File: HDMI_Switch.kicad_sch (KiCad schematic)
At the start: 16 parts, among them U7 HD3SS215RTQR

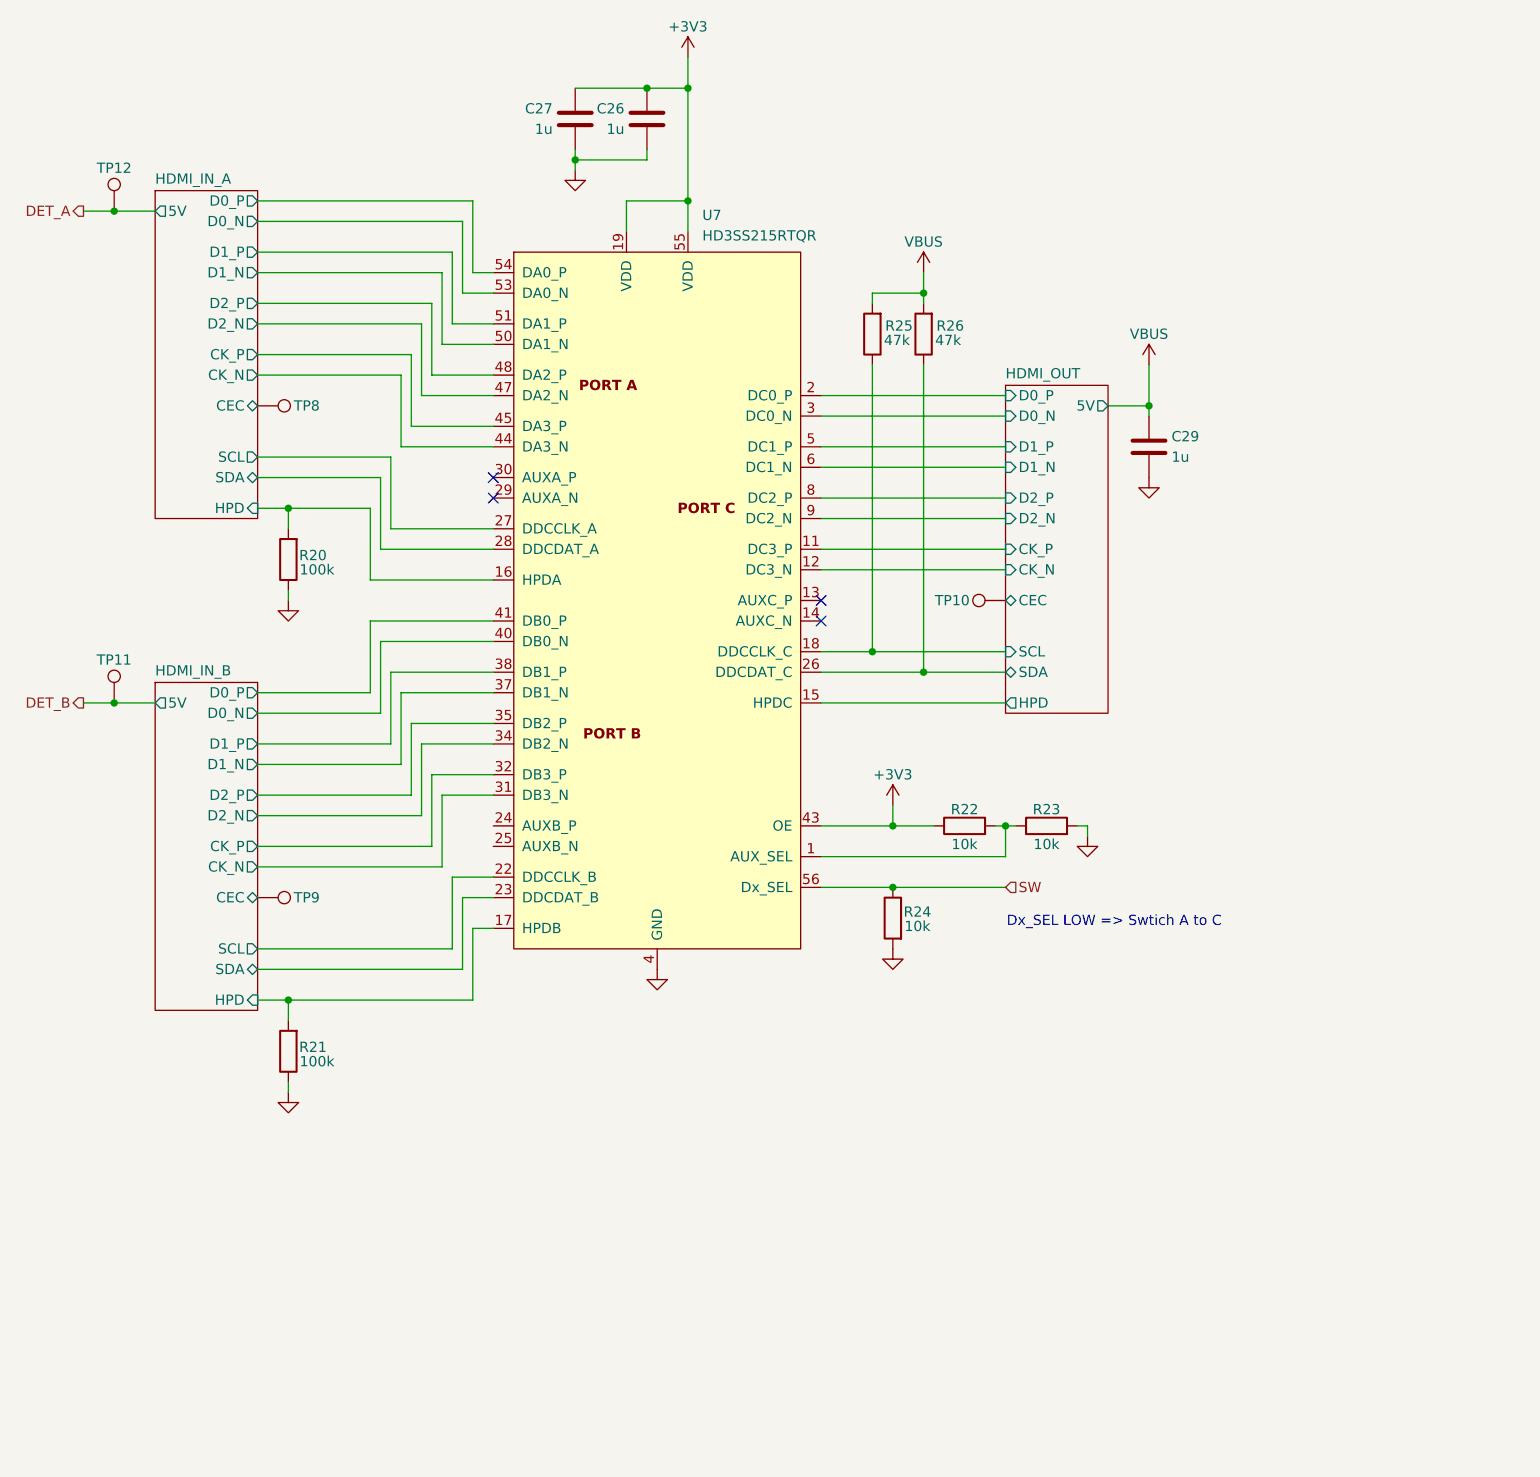
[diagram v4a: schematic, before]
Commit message: Fixed DRC & Adnotations
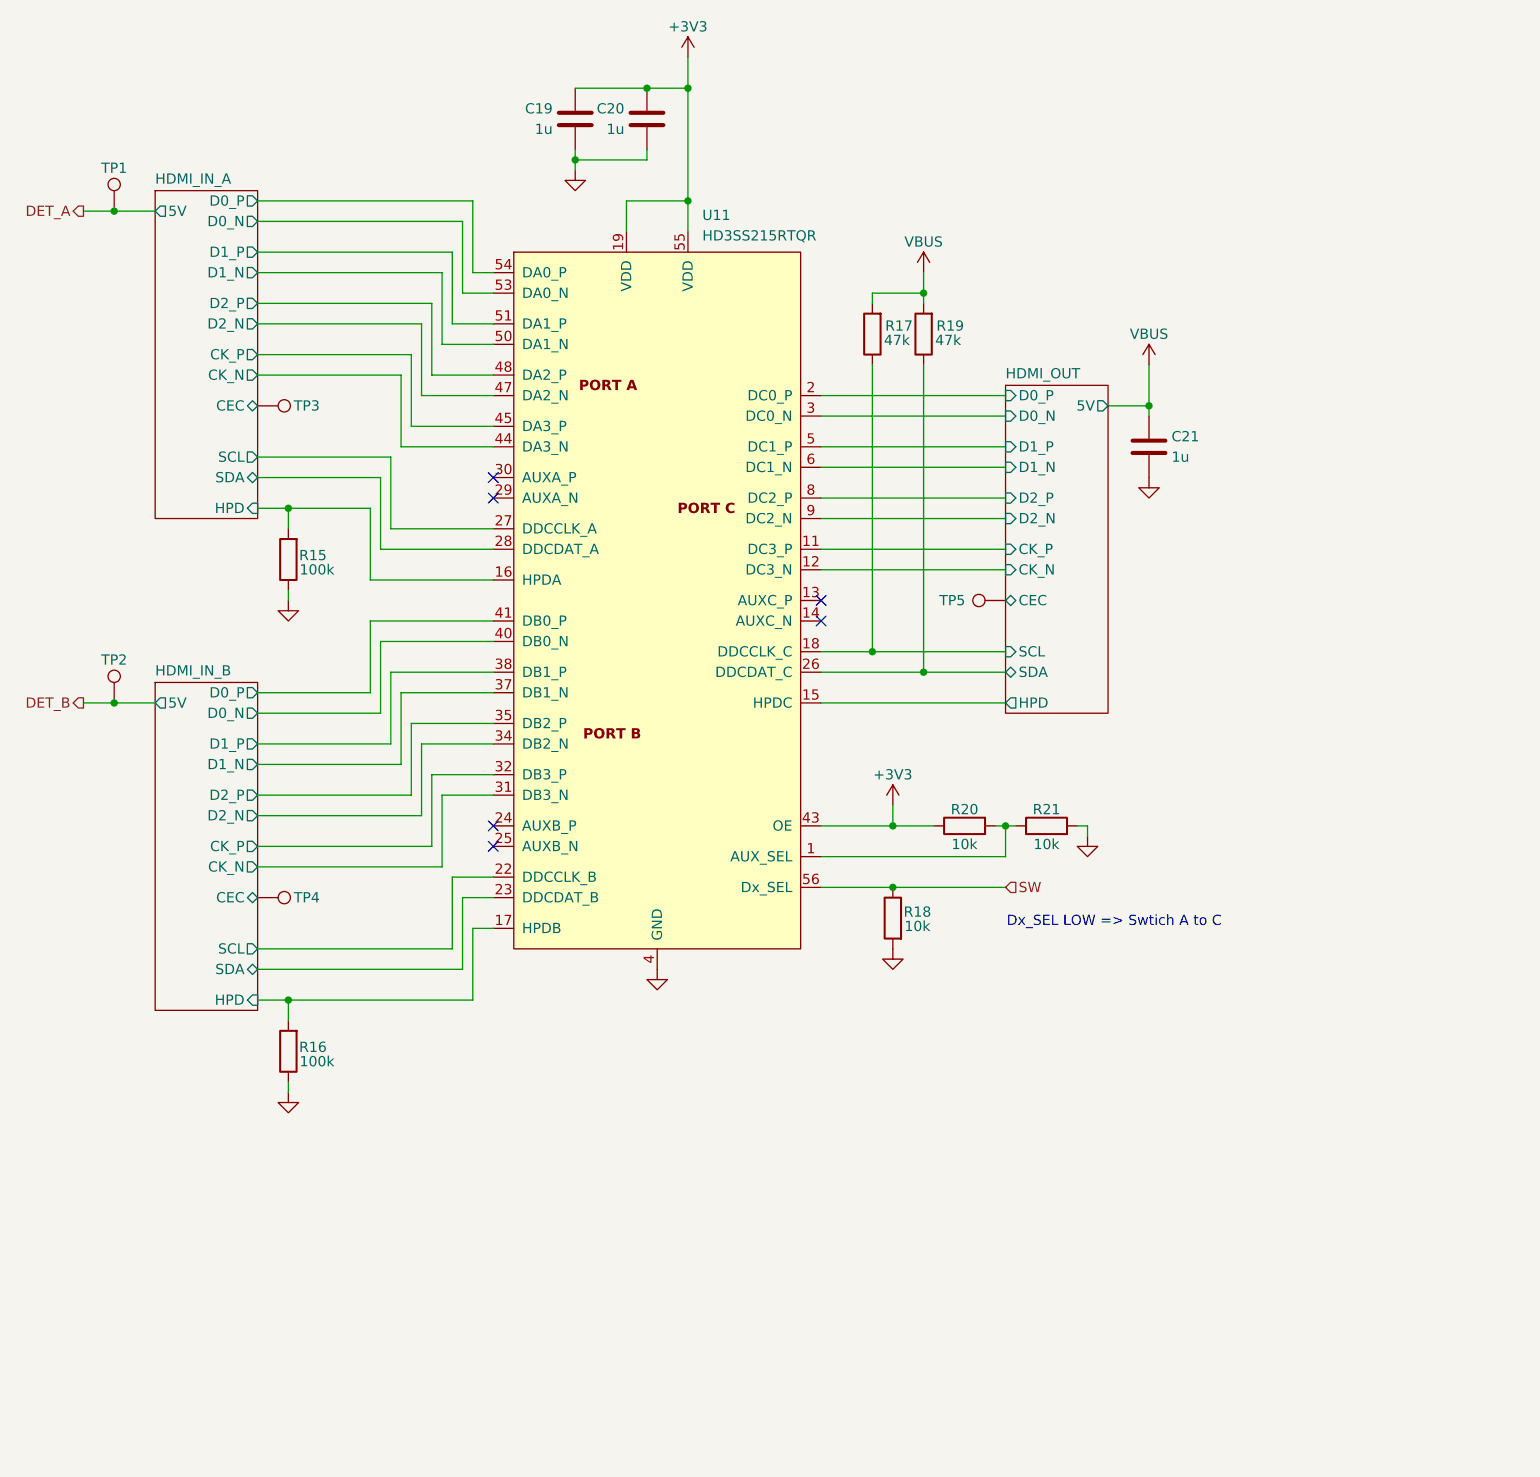
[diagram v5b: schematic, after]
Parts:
- renumbered C27 to C19, C26 to C20, C29 to C21, R20 to R15, R21 to R16, R25 to R17, R24 to R18, R26 to R19, R22 to R20, R23 to R21, TP12 to TP1, TP11 to TP2, TP8 to TP3, TP9 to TP4, TP10 to TP5, U7 to U11
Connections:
- no-connect marks 4 -> 6
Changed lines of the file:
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@@
 	)
 	(no_connect
+		(at 118.11 124.46)
+	)
+	(no_connect
 		(at 158.75 96.52)
 	)
@@
 		(at 158.75 99.06)
 	)
+	(no_connect
+		(at 118.11 127)
+	)
 	(wire
 		(pts
@@
 		(in_pos_files yes)
 		(dnp no)
-		(property "Reference" "#PWR054"
+		(property "Reference" "#PWR027"
 			(at 142.24 33.02 0)
 			(hide yes)
@@
 			(project "KVM_Switch"
 				(path "/94386106-ccd4-487f-b5c5-d52ec3dd59db/6e43926c-16e0-4a92-a7fc-ce5a89c8ce59"
-					(reference "#PWR054")
+					(reference "#PWR027")
 					(unit 1)
 				)
@@
 		(in_pos_files yes)
 		(dnp no)
-		(property "Reference" "C27"
+		(property "Reference" "C19"
 			(at 125.476 35.56 0)
 			(show_name no)
@@
 			(project "KVM_Switch"
 				(path "/94386106-ccd4-487f-b5c5-d52ec3dd59db/6e43926c-16e0-4a92-a7fc-ce5a89c8ce59"
-					(reference "C27")
+					(reference "C19")
 					(unit 1)
 				)
@@
 		(in_pos_files yes)
 		(dnp no)
-		(property "Reference" "C29"
+		(property "Reference" "C21"
 			(at 202.184 76.2 0)
 			(show_name no)
@@
 			(project "KVM_Switch"
 				(path "/94386106-ccd4-487f-b5c5-d52ec3dd59db/6e43926c-16e0-4a92-a7fc-ce5a89c8ce59"
-					(reference "C29")
+					(reference "C21")
 					(unit 1)
 				)
@@
 		(in_pos_files yes)
 		(dnp no)
-		(property "Reference" "TP12"
+		(property "Reference" "TP1"
 			(at 71.12 42.926 0)
 			(show_name no)
@@
 			(project "KVM_Switch"
 				(path "/94386106-ccd4-487f-b5c5-d52ec3dd59db/6e43926c-16e0-4a92-a7fc-ce5a89c8ce59"
-					(reference "TP12")
+					(reference "TP1")
 					(unit 1)
 				)
@@
 		(in_pos_files yes)
 		(dnp no)
-		(property "Reference" "R24"
+		(property "Reference" "R18"
 			(at 170.688 135.128 0)
 			(show_name no)
@@
 			(project "KVM_Switch"
 				(path "/94386106-ccd4-487f-b5c5-d52ec3dd59db/6e43926c-16e0-4a92-a7fc-ce5a89c8ce59"
-					(reference "R24")
+					(reference "R18")
 					(unit 1)
 				)
@@
 		(in_pos_files yes)
 		(dnp no)
-		(property "Reference" "#PWR078"
+		(property "Reference" "#PWR031"
 			(at 191.77 132.08 0)
 			(hide yes)
@@
 			(project "KVM_Switch"
 				(path "/94386106-ccd4-487f-b5c5-d52ec3dd59db/6e43926c-16e0-4a92-a7fc-ce5a89c8ce59"
-					(reference "#PWR078")
+					(reference "#PWR031")
 					(unit 1)
 				)
@@
 		(in_pos_files yes)
 		(dnp no)
-		(property "Reference" "#PWR080"
+		(property "Reference" "#PWR033"
 			(at 199.39 87.63 0)
 			(hide yes)
@@
 			(project "KVM_Switch"
 				(path "/94386106-ccd4-487f-b5c5-d52ec3dd59db/6e43926c-16e0-4a92-a7fc-ce5a89c8ce59"
-					(reference "#PWR080")
+					(reference "#PWR033")
 					(unit 1)
 				)
@@
 		(in_pos_files yes)
 		(dnp no)
-		(property "Reference" "TP11"
+		(property "Reference" "TP2"
 			(at 71.12 103.886 0)
 			(show_name no)
@@
 			(project "KVM_Switch"
 				(path "/94386106-ccd4-487f-b5c5-d52ec3dd59db/6e43926c-16e0-4a92-a7fc-ce5a89c8ce59"
-					(reference "TP11")
+					(reference "TP2")
 					(unit 1)
 				)
@@
 		(in_pos_files yes)
 		(dnp no)
-		(property "Reference" "#PWR079"
+		(property "Reference" "#PWR029"
 			(at 167.64 146.05 0)
 			(hide yes)
@@
 			(project "KVM_Switch"
 				(path "/94386106-ccd4-487f-b5c5-d52ec3dd59db/6e43926c-16e0-4a92-a7fc-ce5a89c8ce59"
-					(reference "#PWR079")
+					(reference "#PWR029")
 					(unit 1)
 				)
@@
 		(in_pos_files yes)
 		(dnp no)
-		(property "Reference" "#PWR057"
+		(property "Reference" "#PWR030"
 			(at 171.45 59.69 0)
 			(hide yes)
@@
 			(project "KVM_Switch"
 				(path "/94386106-ccd4-487f-b5c5-d52ec3dd59db/6e43926c-16e0-4a92-a7fc-ce5a89c8ce59"
-					(reference "#PWR057")
+					(reference "#PWR030")
 					(unit 1)
 				)
@@
 		(in_pos_files yes)
 		(dnp no)
-		(property "Reference" "TP10"
+		(property "Reference" "TP5"
 			(at 175.006 96.52 90)
 			(show_name no)
@@
 			(project "KVM_Switch"
 				(path "/94386106-ccd4-487f-b5c5-d52ec3dd59db/6e43926c-16e0-4a92-a7fc-ce5a89c8ce59"
-					(reference "TP10")
+					(reference "TP5")
 					(unit 1)
 				)
@@
 		(in_pos_files yes)
 		(dnp no)
-		(property "Reference" "#PWR073"
+		(property "Reference" "#PWR026"
 			(at 138.43 148.59 0)
 			(hide yes)
@@
 			(project "KVM_Switch"
 				(path "/94386106-ccd4-487f-b5c5-d52ec3dd59db/6e43926c-16e0-4a92-a7fc-ce5a89c8ce59"
-					(reference "#PWR073")
+					(reference "#PWR026")
 					(unit 1)
 				)
@@
 		(in_pos_files yes)
 		(dnp no)
-		(property "Reference" "#PWR072"
+		(property "Reference" "#PWR024"
 			(at 92.71 163.83 0)
 			(hide yes)
@@
 			(project "KVM_Switch"
 				(path "/94386106-ccd4-487f-b5c5-d52ec3dd59db/6e43926c-16e0-4a92-a7fc-ce5a89c8ce59"
-					(reference "#PWR072")
+					(reference "#PWR024")
 					(unit 1)
 				)
@@
 		(in_pos_files yes)
 		(dnp no)
-		(property "Reference" "TP9"
+		(property "Reference" "TP4"
 			(at 94.996 133.35 90)
 			(show_name no)
@@
 			(project "KVM_Switch"
 				(path "/94386106-ccd4-487f-b5c5-d52ec3dd59db/6e43926c-16e0-4a92-a7fc-ce5a89c8ce59"
-					(reference "TP9")
+					(reference "TP4")
 					(unit 1)
 				)
@@
 		(in_pos_files yes)
 		(dnp no)
-		(property "Reference" "R20"
+		(property "Reference" "R15"
 			(at 95.758 90.932 0)
 			(show_name no)
@@
 			(project "KVM_Switch"
 				(path "/94386106-ccd4-487f-b5c5-d52ec3dd59db/6e43926c-16e0-4a92-a7fc-ce5a89c8ce59"
-					(reference "R20")
+					(reference "R15")
 					(unit 1)
 				)
@@
 		(in_pos_files yes)
 		(dnp no)
-		(property "Reference" "#PWR074"
+		(property "Reference" "#PWR025"
 			(at 128.27 49.53 0)
 			(hide yes)
@@
 			(project "KVM_Switch"
 				(path "/94386106-ccd4-487f-b5c5-d52ec3dd59db/6e43926c-16e0-4a92-a7fc-ce5a89c8ce59"
-					(reference "#PWR074")
+					(reference "#PWR025")
 					(unit 1)
 				)
@@
 		(in_pos_files yes)
 		(dnp no)
-		(property "Reference" "R21"
+		(property "Reference" "R16"
 			(at 95.758 151.892 0)
 			(show_name no)
@@
 			(project "KVM_Switch"
 				(path "/94386106-ccd4-487f-b5c5-d52ec3dd59db/6e43926c-16e0-4a92-a7fc-ce5a89c8ce59"
-					(reference "R21")
+					(reference "R16")
 					(unit 1)
 				)
@@
 		(in_pos_files yes)
 		(dnp no)
-		(property "Reference" "R23"
+		(property "Reference" "R21"
 			(at 186.69 122.428 90)
 			(show_name no)
@@
 			(project "KVM_Switch"
 				(path "/94386106-ccd4-487f-b5c5-d52ec3dd59db/6e43926c-16e0-4a92-a7fc-ce5a89c8ce59"
-					(reference "R23")
+					(reference "R21")
 					(unit 1)
 				)
@@
 		(in_pos_files yes)
 		(dnp no)
-		(property "Reference" "U7"
+		(property "Reference" "U11"
 			(at 144.018 48.768 0)
 			(show_name no)
@@
 			(project "KVM_Switch"
 				(path "/94386106-ccd4-487f-b5c5-d52ec3dd59db/6e43926c-16e0-4a92-a7fc-ce5a89c8ce59"
-					(reference "U7")
+					(reference "U11")
 					(unit 1)
 				)
@@
 		(in_pos_files yes)
 		(dnp no)
-		(property "Reference" "TP8"
+		(property "Reference" "TP3"
 			(at 94.996 72.39 90)
 			(show_name no)
@@
 			(project "KVM_Switch"
 				(path "/94386106-ccd4-487f-b5c5-d52ec3dd59db/6e43926c-16e0-4a92-a7fc-ce5a89c8ce59"
-					(reference "TP8")
+					(reference "TP3")
 					(unit 1)
 				)
@@
 		(in_pos_files yes)
 		(dnp no)
-		(property "Reference" "#PWR055"
+		(property "Reference" "#PWR032"
 			(at 199.39 71.12 0)
 			(hide yes)
@@
 			(project "KVM_Switch"
 				(path "/94386106-ccd4-487f-b5c5-d52ec3dd59db/6e43926c-16e0-4a92-a7fc-ce5a89c8ce59"
-					(reference "#PWR055")
+					(reference "#PWR032")
 					(unit 1)
 				)
@@
 		(in_pos_files yes)
 		(dnp no)
-		(property "Reference" "#PWR056"
+		(property "Reference" "#PWR028"
 			(at 167.64 125.73 0)
 			(hide yes)
@@
 			(project "KVM_Switch"
 				(path "/94386106-ccd4-487f-b5c5-d52ec3dd59db/6e43926c-16e0-4a92-a7fc-ce5a89c8ce59"
-					(reference "#PWR056")
+					(reference "#PWR028")
 					(unit 1)
 				)
@@
 		(in_pos_files yes)
 		(dnp no)
-		(property "Reference" "R25"
+		(property "Reference" "R17"
 			(at 168.402 62.484 0)
 			(show_name no)
@@
 			(project "KVM_Switch"
 				(path "/94386106-ccd4-487f-b5c5-d52ec3dd59db/6e43926c-16e0-4a92-a7fc-ce5a89c8ce59"
-					(reference "R25")
+					(reference "R17")
 					(unit 1)
 				)
@@
 		(in_pos_files yes)
 		(dnp no)
-		(property "Reference" "C26"
+		(property "Reference" "C20"
 			(at 134.366 35.56 0)
 			(show_name no)
@@
 			(project "KVM_Switch"
 				(path "/94386106-ccd4-487f-b5c5-d52ec3dd59db/6e43926c-16e0-4a92-a7fc-ce5a89c8ce59"
-					(reference "C26")
+					(reference "C20")
 					(unit 1)
 				)
@@
 		(in_pos_files yes)
 		(dnp no)
-		(property "Reference" "#PWR071"
+		(property "Reference" "#PWR023"
 			(at 92.71 102.87 0)
 			(hide yes)
@@
 			(project "KVM_Switch"
 				(path "/94386106-ccd4-487f-b5c5-d52ec3dd59db/6e43926c-16e0-4a92-a7fc-ce5a89c8ce59"
-					(reference "#PWR071")
+					(reference "#PWR023")
 					(unit 1)
 				)
@@
 		(in_pos_files yes)
 		(dnp no)
-		(property "Reference" "R22"
+		(property "Reference" "R20"
 			(at 176.53 122.428 90)
 			(show_name no)
@@
 			(project "KVM_Switch"
 				(path "/94386106-ccd4-487f-b5c5-d52ec3dd59db/6e43926c-16e0-4a92-a7fc-ce5a89c8ce59"
-					(reference "R22")
+					(reference "R20")
 					(unit 1)
 				)
@@
 		(in_pos_files yes)
 		(dnp no)
-		(property "Reference" "R26"
+		(property "Reference" "R19"
 			(at 174.752 62.484 0)
 			(show_name no)
@@
 			(project "KVM_Switch"
 				(path "/94386106-ccd4-487f-b5c5-d52ec3dd59db/6e43926c-16e0-4a92-a7fc-ce5a89c8ce59"
-					(reference "R26")
+					(reference "R19")
 					(unit 1)
 				)
